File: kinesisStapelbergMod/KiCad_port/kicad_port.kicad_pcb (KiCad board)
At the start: 2 copper layers, 15 parts, among them J1 Conn_01x13, J2 Conn_01x13, J3 Conn_01x13, J4 Conn_01x13, J5 Conn_01x10, J6 Conn_01x10, U1 Teensy++_2_0

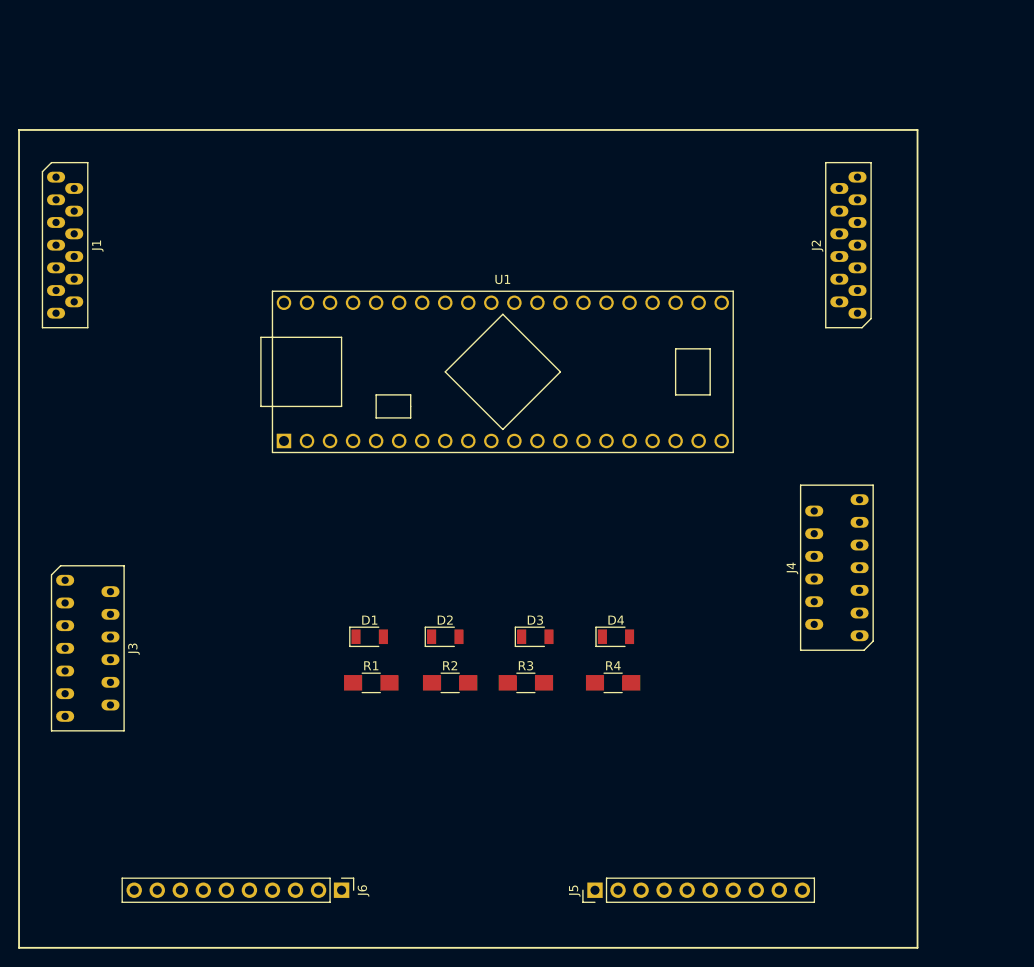
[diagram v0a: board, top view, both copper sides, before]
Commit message: change LED and Resistor footprints
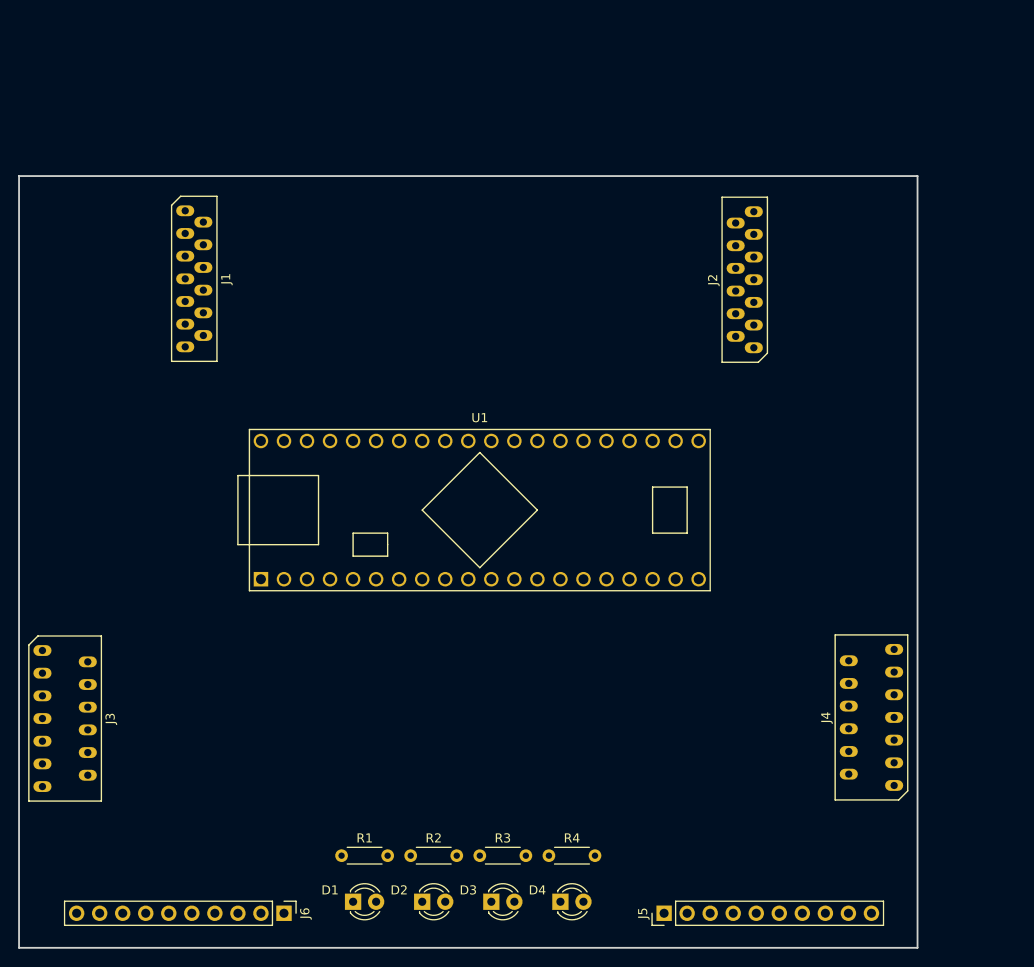
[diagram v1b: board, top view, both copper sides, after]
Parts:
- D1, D2, D3, D4: footprint Diodes_SMD:D_1206 -> LED_THT:LED_D3.0mm
- R1, R2, R3, R4: footprint Resistors_SMD:R_1206_HandSoldering -> Resistor_THT:R_Axial_DIN0204_L3.6mm_D1.6mm_P5.08mm_Horizontal
- moved D4 29.8 mm to (149.9, 147.3)
- moved D3 29.6 mm to (142.2, 147.3)
- moved D2 29.3 mm to (134.6, 147.3)
- moved D1 29.3 mm to (127.0, 147.3)
- moved R4 20.3 mm to (148.6, 142.2)
- moved R3 19.7 mm to (141.0, 142.2)
- moved R2 19.5 mm to (133.3, 142.2)
- moved R1 19.3 mm to (125.7, 142.2)
- moved J4 16.9 mm to (184.2, 127.0)
- moved U1 15.5 mm to (141.0, 104.1)
- moved J1 14.7 mm to (109.5, 78.6)
- moved J2 12.0 mm to (170.2, 78.7)
- moved J3 8.13 mm to (95.2, 127.1)
- moved J5 8.03 mm to (161.3, 148.6)
- moved J6 6.84 mm to (119.4, 148.6)
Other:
- board outline added: 99.1 x 85.1 mm

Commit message: modify led position
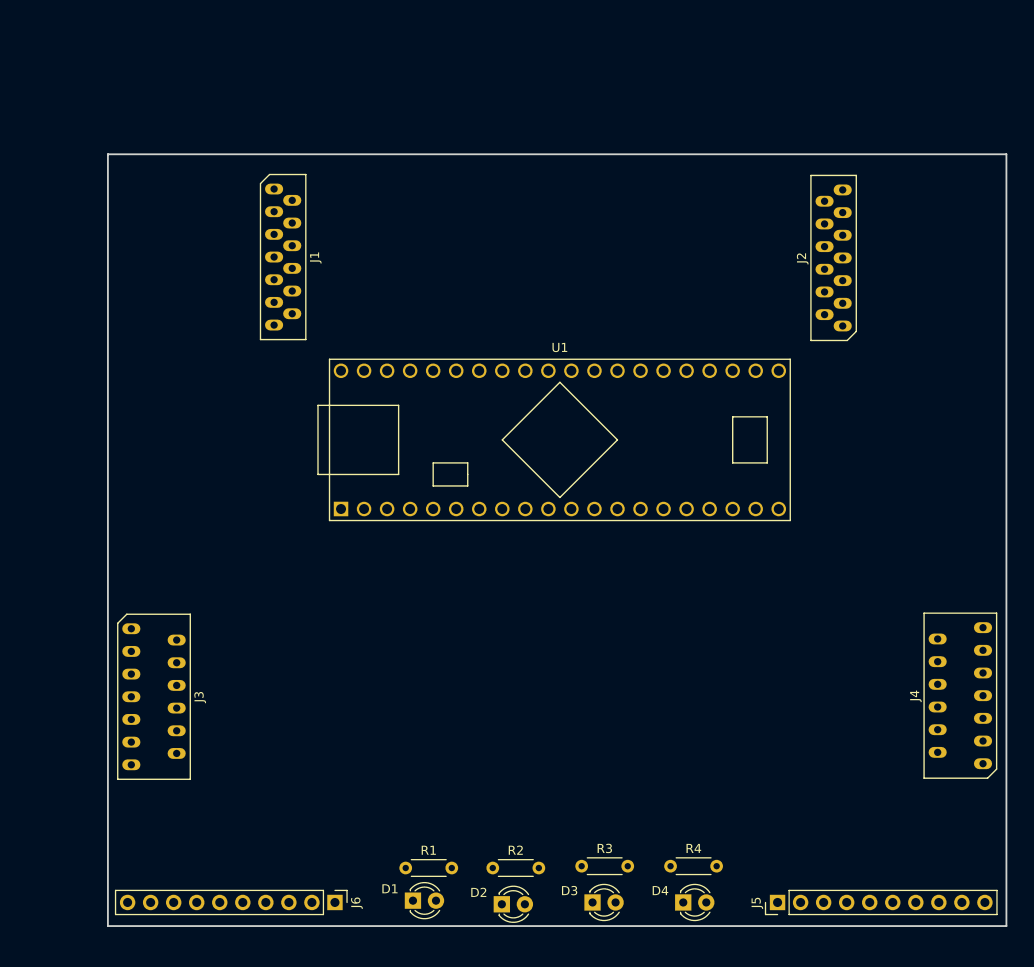
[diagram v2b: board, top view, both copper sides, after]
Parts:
- moved D4 13.5 mm to (163.4, 147.4)
- moved R4 13.5 mm to (162.0, 143.4)
- moved J5 12.6 mm to (173.8, 147.4)
- moved U1 11.7 mm to (149.8, 96.4)
- moved R3 11.3 mm to (152.2, 143.4)
- moved D3 11.2 mm to (153.4, 147.4)
- moved J1 10.1 mm to (119.3, 76.2)
- moved J3 10.1 mm to (105.0, 124.7)
- moved J4 10.1 mm to (193.9, 124.6)
- moved J2 10.1 mm to (180.0, 76.3)
- moved R2 9.15 mm to (142.4, 143.6)
- moved D2 8.78 mm to (143.4, 147.6)
- moved R1 7.20 mm to (132.8, 143.6)
- moved D1 6.60 mm to (133.6, 147.2)
- moved J6 5.74 mm to (125.0, 147.4)
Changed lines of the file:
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@@
   )
   (module kinesisMod_board_connectors:Molex_0039532135 (layer F.Cu)
-    (at 109.49 78.64 270)
+    (at 119.29 76.24 270)
     (fp_text reference J1 (at 0 -3.5 270) (layer F.SilkS)
       (effects (font (size 1 1) (thickness 0.15)))
@@
   )
   (module kinesisMod_board_connectors:Molex_0039532135 (layer F.Cu)
-    (at 170.18 78.74 90)
+    (at 179.98 76.34 90)
     (fp_text reference J2 (at 0 -3.5 90) (layer F.SilkS)
       (effects (font (size 1 1) (thickness 0.15)))
@@
   )
   (module kinesisMod_board_connectors:Molex_039532134 (layer F.Cu)
-    (at 95.25 127.12 270)
+    (at 105.05 124.72 270)
     (fp_text reference J3 (at 0 -5 270) (layer F.SilkS)
       (effects (font (size 1 1) (thickness 0.15)))
@@
   )
   (module kinesisMod_board_connectors:Molex_039532134 (layer F.Cu)
-    (at 184.15 127 90)
+    (at 193.95 124.6 90)
     (fp_text reference J4 (at 0 -5 90) (layer F.SilkS)
       (effects (font (size 1 1) (thickness 0.15)))
@@
   )
   (module Pin_Headers:Pin_Header_Straight_1x10_Pitch2.54mm (layer F.Cu)
-    (at 161.29 148.59 90)
+    (at 173.8 147.4 90)
     (descr "Through hole straight pin header, 1x10, 2.54mm pitch, single row")
     (tags "Through hole pin header THT 1x10 2.54mm single row")
@@
   )
   (module Pin_Headers:Pin_Header_Straight_1x10_Pitch2.54mm (layer F.Cu)
-    (at 119.38 148.59 270)
+    (at 125 147.4 270)
     (descr "Through hole straight pin header, 1x10, 2.54mm pitch, single row")
     (tags "Through hole pin header THT 1x10 2.54mm single row")
@@
   )
   (module teensy:Teensy++_2_0_40p (layer F.Cu)
-    (at 140.97 104.14)
+    (at 149.8 96.4)
     (descr 20)
     (fp_text reference U1 (at 0 -10.16) (layer F.SilkS)
@@
   )
   (module LED_THT:LED_D3.0mm (layer F.Cu)
-    (at 127 147.32)
+    (at 133.6 147.2)
     (descr "LED, diameter 3.0mm, 2 pins")
     (tags "LED diameter 3.0mm 2 pins")
@@
   )
   (module LED_THT:LED_D3.0mm (layer F.Cu)
-    (at 134.62 147.32)
+    (at 143.4 147.6)
     (descr "LED, diameter 3.0mm, 2 pins")
     (tags "LED diameter 3.0mm 2 pins")
@@
   )
   (module LED_THT:LED_D3.0mm (layer F.Cu)
-    (at 142.24 147.32)
+    (at 153.4 147.4)
     (descr "LED, diameter 3.0mm, 2 pins")
     (tags "LED diameter 3.0mm 2 pins")
@@
   )
   (module LED_THT:LED_D3.0mm (layer F.Cu)
-    (at 149.86 147.32)
+    (at 163.4 147.4)
     (descr "LED, diameter 3.0mm, 2 pins")
     (tags "LED diameter 3.0mm 2 pins")
@@
   )
   (module Resistor_THT:R_Axial_DIN0204_L3.6mm_D1.6mm_P5.08mm_Horizontal (layer F.Cu)
-    (at 125.73 142.24)
+    (at 132.8 143.6)
     (descr "Resistor, Axial_DIN0204 series, Axial, Horizontal, pin pitch=5.08mm, 0.167W, length*diameter=3.6*1.6mm^2, http://cdn-reichelt.de/documents/datenblatt/B400/1_4W%23YAG.pdf")
     (tags "Resistor Axial_DIN0204 series Axial Horizontal pin pitch 5.08mm 0.167W length 3.6mm diameter 1.6mm")
@@
   )
   (module Resistor_THT:R_Axial_DIN0204_L3.6mm_D1.6mm_P5.08mm_Horizontal (layer F.Cu)
-    (at 133.35 142.24)
+    (at 142.4 143.6)
     (descr "Resistor, Axial_DIN0204 series, Axial, Horizontal, pin pitch=5.08mm, 0.167W, length*diameter=3.6*1.6mm^2, http://cdn-reichelt.de/documents/datenblatt/B400/1_4W%23YAG.pdf")
     (tags "Resistor Axial_DIN0204 series Axial Horizontal pin pitch 5.08mm 0.167W length 3.6mm diameter 1.6mm")
@@
   )
   (module Resistor_THT:R_Axial_DIN0204_L3.6mm_D1.6mm_P5.08mm_Horizontal (layer F.Cu)
-    (at 140.97 142.24)
+    (at 152.2 143.4)
     (descr "Resistor, Axial_DIN0204 series, Axial, Horizontal, pin pitch=5.08mm, 0.167W, length*diameter=3.6*1.6mm^2, http://cdn-reichelt.de/documents/datenblatt/B400/1_4W%23YAG.pdf")
     (tags "Resistor Axial_DIN0204 series Axial Horizontal pin pitch 5.08mm 0.167W length 3.6mm diameter 1.6mm")
@@
   )
   (module Resistor_THT:R_Axial_DIN0204_L3.6mm_D1.6mm_P5.08mm_Horizontal (layer F.Cu)
-    (at 148.59 142.24)
+    (at 162 143.4)
     (descr "Resistor, Axial_DIN0204 series, Axial, Horizontal, pin pitch=5.08mm, 0.167W, length*diameter=3.6*1.6mm^2, http://cdn-reichelt.de/documents/datenblatt/B400/1_4W%23YAG.pdf")
     (tags "Resistor Axial_DIN0204 series Axial Horizontal pin pitch 5.08mm 0.167W length 3.6mm diameter 1.6mm")
@@
     )
   )
-  (gr_line (start 90.17 67.31) (end 90.17 152.4) (layer Edge.Cuts) (width 0.2))
-  (gr_line (start 189.23 67.31) (end 90.17 67.31) (layer Edge.Cuts) (width 0.2))
-  (gr_line (start 189.23 152.4) (end 189.23 67.31) (layer Edge.Cuts) (width 0.2))
-  (gr_line (start 90.17 152.4) (end 189.23 152.4) (layer Edge.Cuts) (width 0.2))
+  (gr_line (start 99.97 64.91) (end 99.97 150) (layer Edge.Cuts) (width 0.2))
+  (gr_line (start 199.03 64.91) (end 99.97 64.91) (layer Edge.Cuts) (width 0.2))
+  (gr_line (start 199.03 150) (end 199.03 64.91) (layer Edge.Cuts) (width 0.2))
+  (gr_line (start 99.97 150) (end 199.03 150) (layer Edge.Cuts) (width 0.2))
 )

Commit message: add dimensions to converted board, transferred to ported board
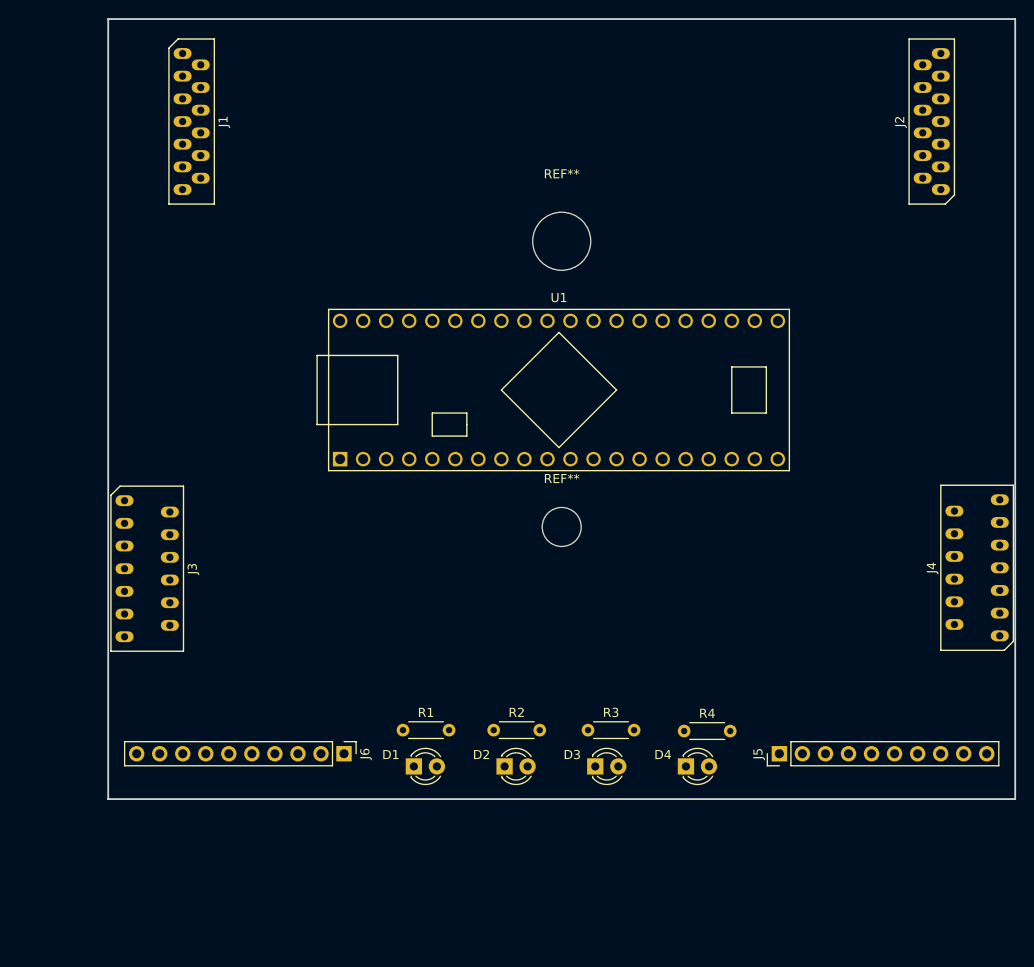
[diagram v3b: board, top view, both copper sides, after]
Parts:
- added REF**: MountingHole_4.3mm_M4, Mounting_Holes:MountingHole_4.3mm_M4, F.Cu at (150.0, 106.0)
- added REF**: MountingHole_6.4mm_M6, Mounting_Holes:MountingHole_6.4mm_M6, F.Cu at (150.0, 74.5)
- moved J2 18.5 mm to (190.8, 61.3)
- moved J1 18.0 mm to (109.2, 61.3)
- moved J6 16.4 mm to (126.0, 131.0)
- moved J5 16.4 mm to (174.0, 131.0)
- moved D2 15.2 mm to (143.7, 132.4)
- moved R1 15.2 mm to (132.5, 128.4)
- moved R2 15.2 mm to (142.5, 128.4)
- moved R3 15.0 mm to (152.9, 128.4)
- moved D3 15.0 mm to (153.7, 132.4)
- moved D4 15.0 mm to (163.7, 132.4)
- moved R4 15.0 mm to (163.5, 128.5)
- moved D1 14.8 mm to (133.7, 132.4)
- moved J4 14.2 mm to (195.8, 110.5)
- moved J3 14.1 mm to (104.3, 110.6)
- moved U1 5.50 mm to (149.7, 90.9)
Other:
- board size 99.1 x 85.1 mm -> 100 x 86 mm
- board text added: "Top Left of Board X: 100 Y: 50"
